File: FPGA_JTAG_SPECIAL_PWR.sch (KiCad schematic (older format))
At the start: 45 parts, among them J2 Reset_Switch, U18 LDL212D33R, U19 TLV75512, U900 GW1N-9LQ100

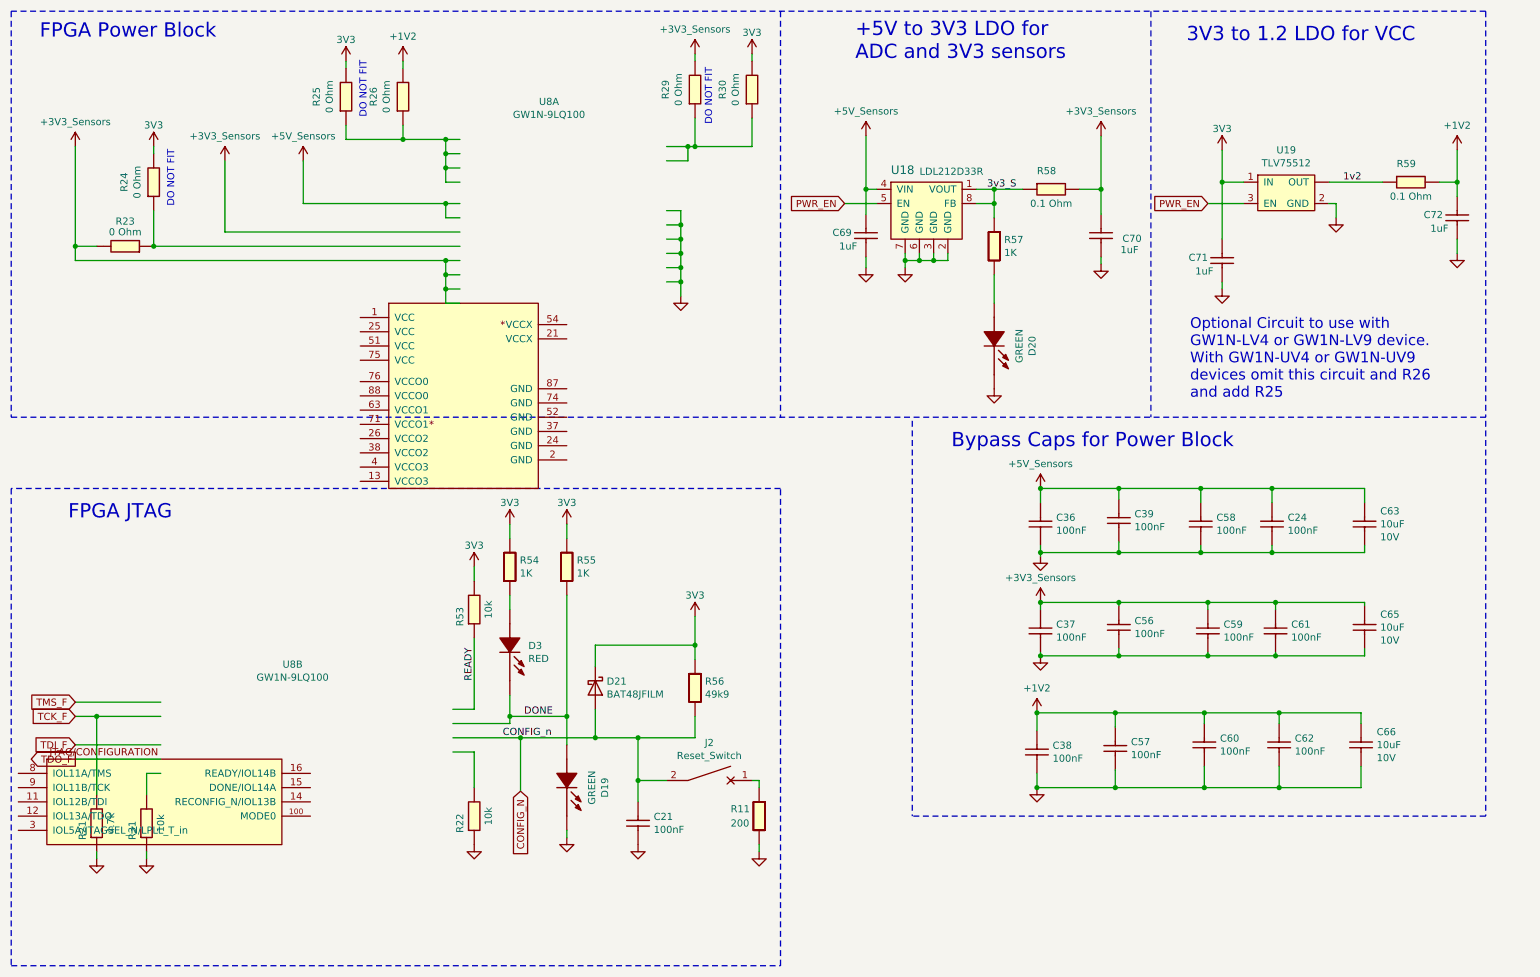
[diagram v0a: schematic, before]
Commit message: Update FPGA symbol, remove FPGA_trial sheet
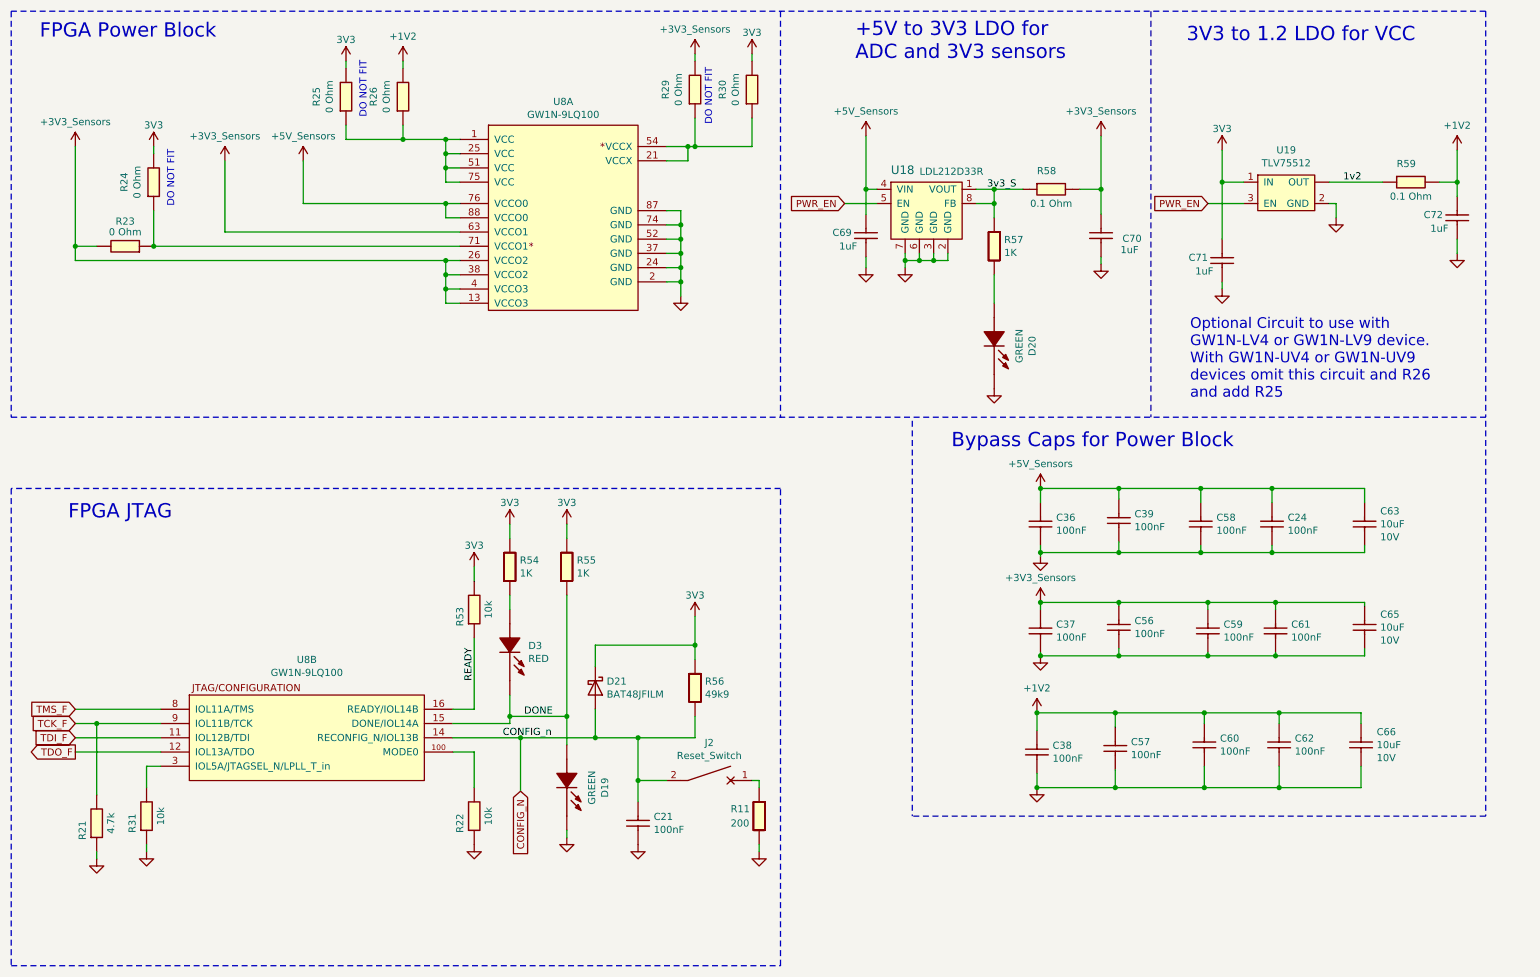
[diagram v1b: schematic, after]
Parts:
- removed U900: GW1N-9LQ100, symbol OpenVent:GW1N-9LQ100
- added U8: GW1N-9LQ100, symbol OpenVent:GW1N-9LQ100
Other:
- moved on the sheet: R31

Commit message: Update FPGA_JTAG_SPECIAL_PWR.sch
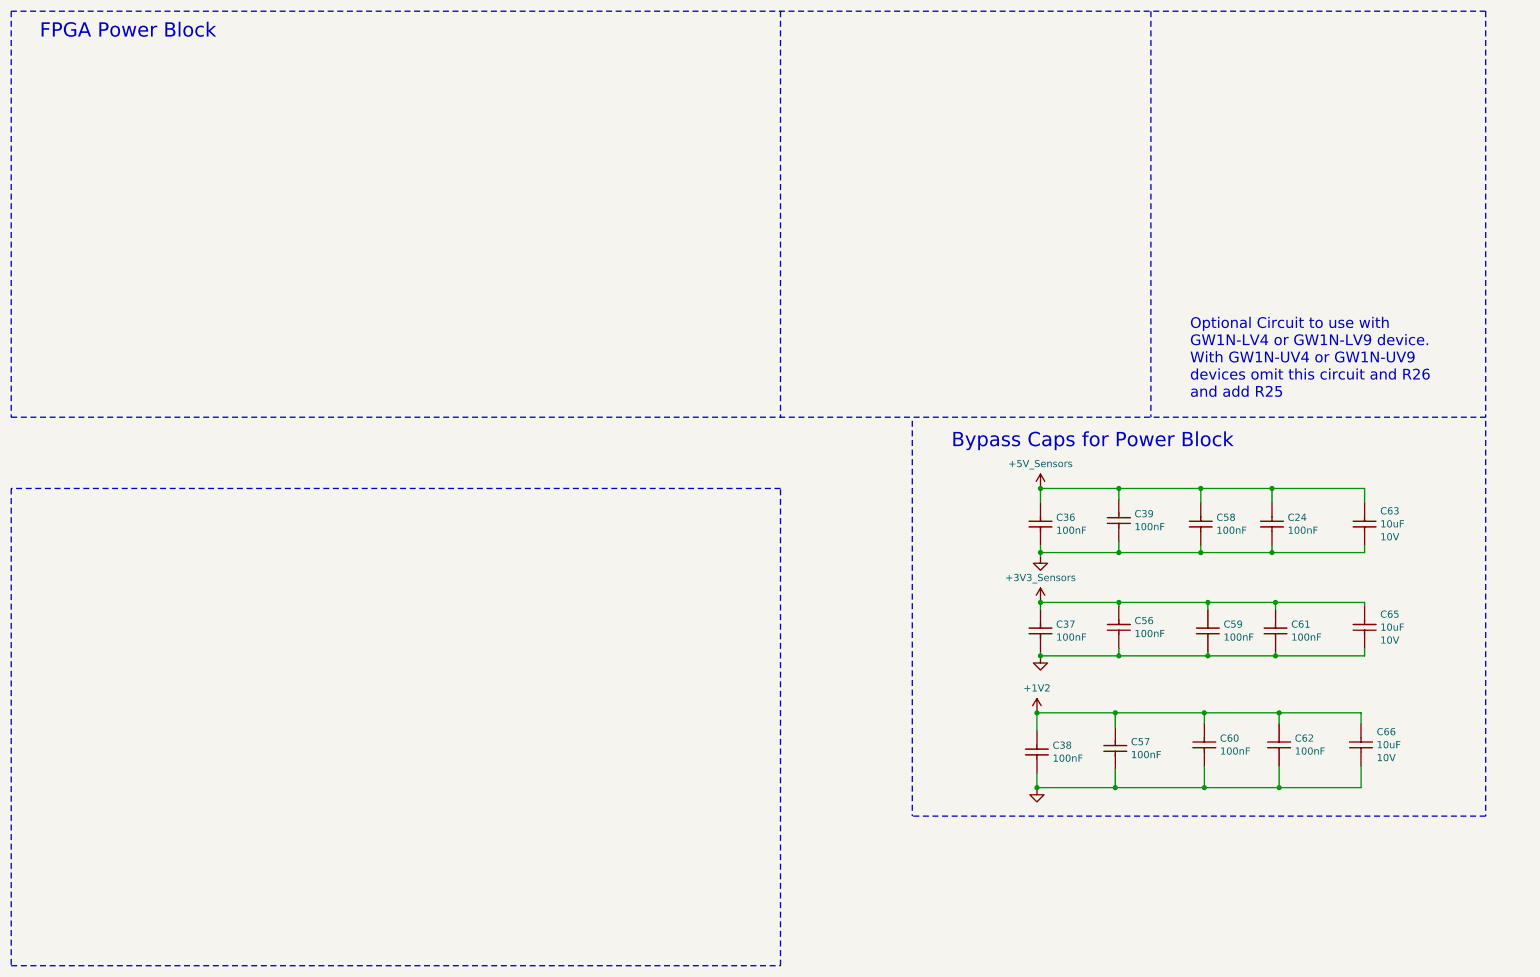
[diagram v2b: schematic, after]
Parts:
- removed C21: 100nF_0603_Ceramic_Capacitor,_10%,_X7R,_25V, symbol OpenVent:100nF_0603_Ceramic_Capacitor,_10%,_X7R,_25V
- removed C69, C70, C71, C72: 1uF_0603_Ceramic_Capacitor,_10%,_50V,_X5R, Capacitor_SMD:C_0603_1608Metric, symbol OpenVent:1uF_0603_Ceramic_Capacitor,_10%,_50V,_X5R
- removed D19, D20: LED_GREEN_0603_SMD, symbol OpenVent:LED_GREEN_0603_SMD
- removed D21: BAT48JFILM, Diode_SMD:D_SOD-323, symbol OpenVent-rescue:BAT48JFILM-Diode
- removed D3: LED_Red_0603_SMD, symbol OpenVent:LED_Red_0603_SMD
- removed J2: Reset_Switch, symbol Device:CircuitBreaker_1P
- removed R1, R31, R53, R81: 12k_0603_Chip_Resistor,_1%,_0.1W, Resistor_SMD:R_0603_1608Metric, symbol OpenVent:12k_0603_Chip_Resistor,_1%,_0.1W
- removed R11: R_0603_200_0.1W_1%, Resistor_SMD:R_0603_1608Metric, symbol OpenVent:R_0603_200_0.1W_1%
- removed R23, R24, R25, R26, R29, R30: 0R0_0603_Chip_Resistor,_1%,_0.1W, symbol OpenVent:0R0_0603_Chip_Resistor,_1%,_0.1W
- removed R54, R55, R57: 1K_0603_Chip_Resistor,_1%,_0.1W, symbol OpenVent:1K_0603_Chip_Resistor,_1%,_0.1W
- removed R56: R_0603_49k9_0.1W_1%, symbol OpenVent:R_0603_49k9_0.1W_1%
- removed R58, R59: 0R1_0603_Chip_Resistor,_1%,_0.1W, Resistor_SMD:R_0603_1608Metric, symbol OpenVent:0R1_0603_Chip_Resistor,_1%,_0.1W
- removed U18: LDL212D33R, Package_SO:SO-8_5.3x6.2mm_P1.27mm, symbol OpenVent:LDL212D33R
- removed U19: TLV75512, symbol OpenVent:TLV75512
- removed U8: GW1N-9LQ100, symbol OpenVent:GW1N-9LQ100
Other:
- note removed: "+5V to 3V3 LDO for \nADC and 3V3 sensors\n"
- note removed: "3V3 to 1.2 LDO for VCC\n"
- note removed: "DO NOT FIT"
- note removed: "FPGA JTAG\n"

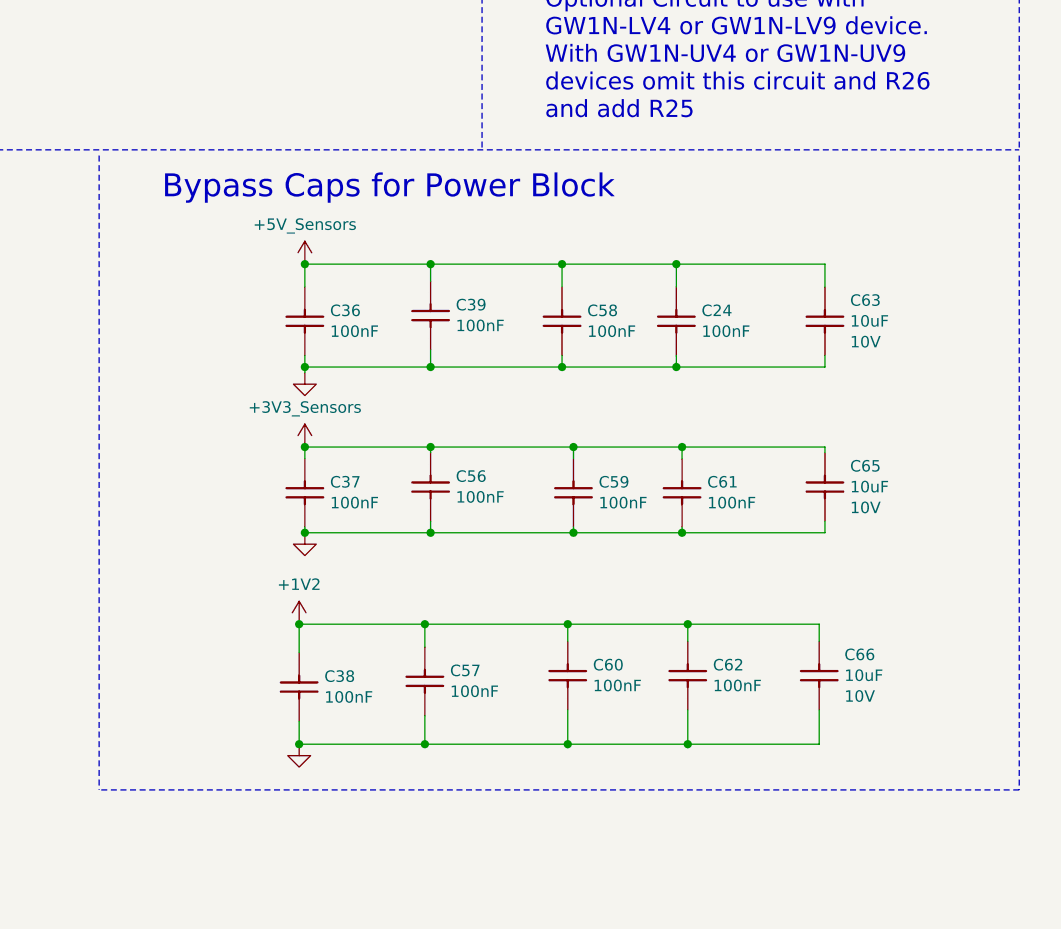
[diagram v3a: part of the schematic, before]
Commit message: Moved FPGA decoupling caps to FPGA sheet. Deleted FPGA JTAG SPECIAL PWR sheet as now empty
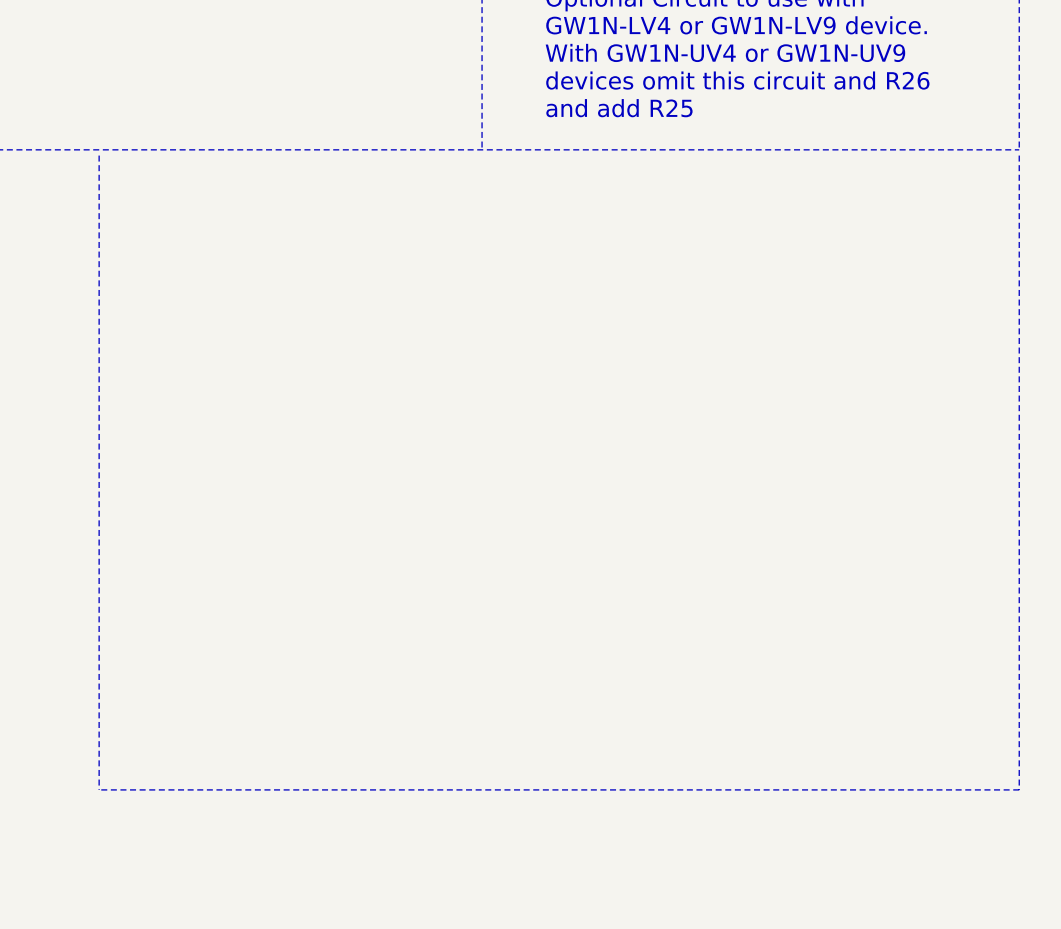
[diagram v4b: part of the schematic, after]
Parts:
- removed C24, C36, C37, C38, C39, C56, C57, C58, C59, C60, C61, C62: 100nF_0603_Ceramic_Capacitor,_10%,_X7R,_25V, symbol OpenVent:100nF_0603_Ceramic_Capacitor,_10%,_X7R,_25V
- removed C63, C65, C66: 10uF_0805_Ceramic_Capacitor_10%_X7R_10V, Capacitor_SMD:C_0805_2012Metric, symbol OpenVent:10uF_0805_Ceramic_Capacitor_10%_X7R_10V
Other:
- note removed: "Bypass Caps for Power Block"
